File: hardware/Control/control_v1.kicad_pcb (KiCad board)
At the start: 2 copper layers, 109.2 x 88.9 mm, 40 parts, among them J1 Conn_02x07_Counter_Clockwise, J2 Screw_Terminal_01x05, J3 Conn_01x06, J4 RJ45, M1 STM32F4-DISCOVERY, U1 TL2575HV-ADJ, U2 TL2575HV-ADJ

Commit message: Updated to rev 2
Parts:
- C1: footprint Capacitor_SMD:CP_Elec_10x10.5 -> Capacitor_THT:CP_Radial_D10.0mm_P5.00mm
- C10, R5, R6: moved to B.Cu
- C2: value 1mF -> 100uF; footprint Capacitor_THT:CP_Radial_D16.0mm_P7.50mm -> Capacitor_THT:CP_Radial_D10.0mm_P5.00mm
- C3: footprint Capacitor_SMD:CP_Elec_8x10 -> Capacitor_THT:CP_Radial_D10.0mm_P5.00mm
- C4: footprint Capacitor_SMD:CP_Elec_10x10 -> Capacitor_THT:CP_Radial_D10.0mm_P5.00mm
- R2, R3: footprint Resistor_SMD:R_0603_1608Metric_Pad1.05x0.95mm_HandSolder -> Resistor_SMD:R_0805_2012Metric_Pad1.33x1.40mm_HandSolder
- moved C10 27.8 mm to (124.5, 89.2)
- moved R6 27.7 mm to (124.5, 92.8)
- moved R5 27.5 mm to (124.6, 85.1), turned to 0 degrees
- moved R11 18.0 mm to (176.1, 119.4)
- moved R12 18.0 mm to (176.1, 123.2)
- moved C8 18.0 mm to (176.1, 115.6)
- moved D1 12.6 mm to (165.0, 84.0), turned to 180 degrees
- moved C4 2.54 mm to (201.9, 125.7)
- moved C3 2.25 mm to (202.8, 95.5)
- moved C2 2.05 mm to (113.8, 119.6)
- moved L1 1.02 mm to (204.3, 79.8), turned to 0 degrees
- turned C5 to 0 degrees
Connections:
- MK1 pad 1: (no net) -> /GND
- MK2 pad 1: (no net) -> /GND
- MK3 pad 1: (no net) -> /GND
- MK4 pad 1: (no net) -> /GND
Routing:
- net /LS_A_TTL_PWM: track 24.8 -> 76.0 mm
- net /LS_C_TTL_PWM: track 20.5 -> 68.8 mm, vias 1 -> 0
- net /PHASEB_FB: track 70.6 -> 23.8 mm, vias 1 -> 2
- net /microcontroller/HALL_B_SENSE: track 22.9 -> 65.4 mm, vias 0 -> 1
- net /LS_B_TTL_PWM: track 31.7 -> 72.5 mm
- net /PHASEA_FB: track 41.1 -> 75.1 mm
- net /5v: track 271.3 -> 244.5 mm
- net /powerconverters/5v_OUT: track 56.3 -> 79.0 mm
- net /12v: track 142.2 -> 163.9 mm
- net /HALL_B: track 47.8 -> 34.4 mm
- net /microcontroller/PC5: track 27.0 -> 15.1 mm
- net /I2C_SCL: track 57.9 -> 68.6 mm, vias 1 -> 0
- net /48v: track 174.6 -> 183.7 mm, vias 4 -> 3
- net /powerconverters/12v_OUT: track 71.3 -> 79.8 mm, vias 1 -> 0
- net /GND: track 0.00 -> 7.19 mm, vias 9 -> 3
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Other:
- board text added: "Alex Simon 3/9/2019 Rev. 2"
- board text removed: "Alex Simon 2/7/2019 Rev. 1"

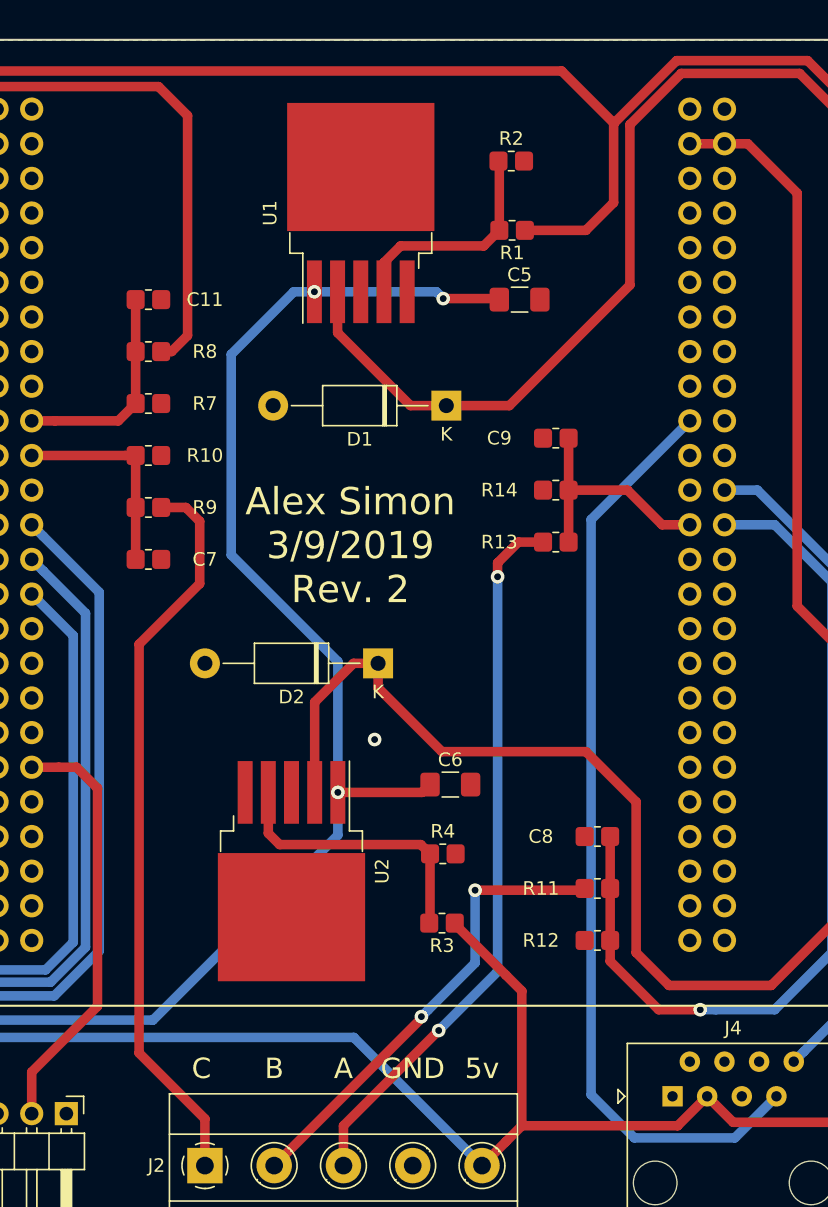
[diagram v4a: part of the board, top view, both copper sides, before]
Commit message: Added Transmission Enable
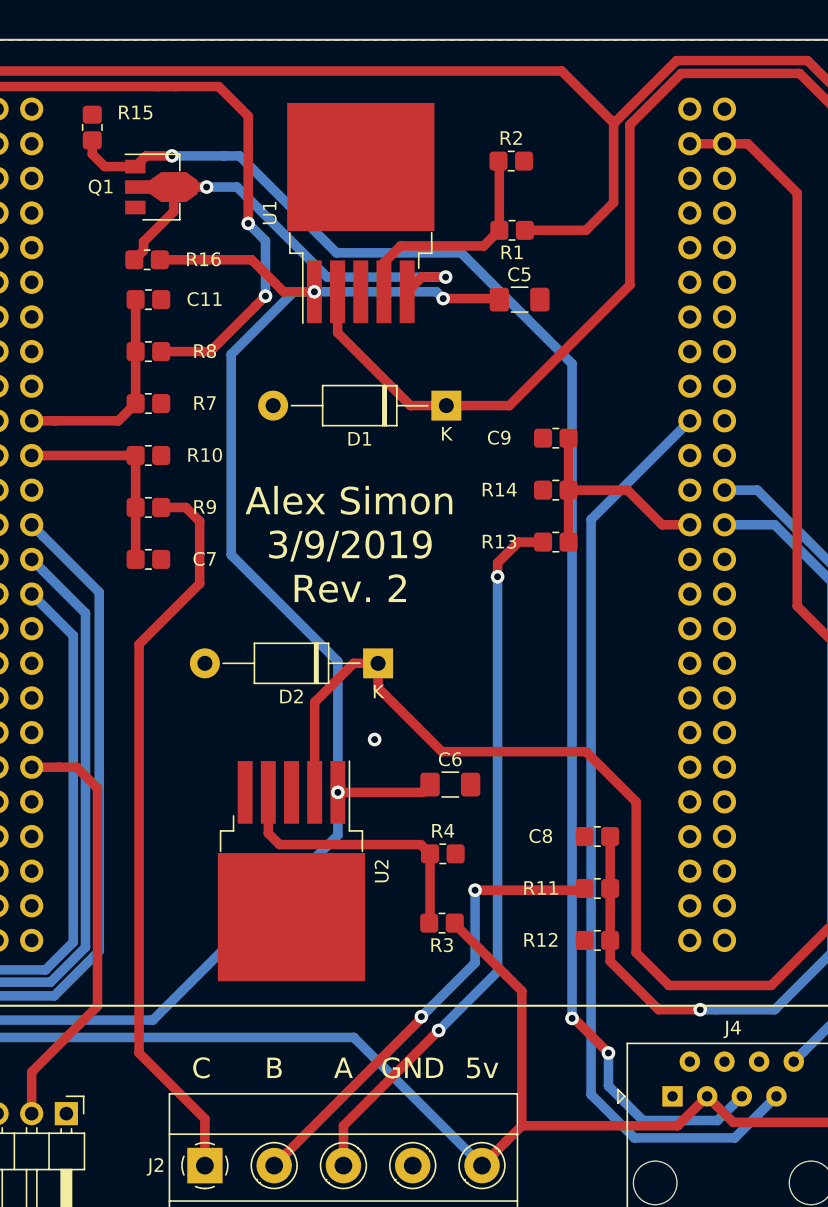
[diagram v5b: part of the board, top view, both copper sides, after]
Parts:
- added Q1: BCX56, Package_TO_SOT_SMD:SOT-89-3, F.Cu at (143.7, 67.9)
- added R15: 2k, Resistor_SMD:R_0805_2012Metric_Pad1.33x1.40mm_HandSolder, F.Cu at (139.1, 63.6)
- added R16: 18k, Resistor_SMD:R_0805_2012Metric_Pad1.33x1.40mm_HandSolder, F.Cu at (143.1, 73.3)
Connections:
- J3 pad 1: Net-(J3-Pad1) -> (no net)
- J3 pad 4: Net-(J3-Pad4) -> (no net)
- J3 pad 5: Net-(J3-Pad5) -> (no net)
- J4 pad 1: Net-(J4-Pad1) -> (no net)
- J4 pad 2: Net-(J4-Pad2) -> (no net)
- J4 pad 4: Net-(J4-Pad4) -> (no net)
- J4 pad 5: Net-(J4-Pad5) -> /TransEnable_TTL
- M1 pad 10: Net-(M1-Pad10) -> (no net)
- M1 pad 12: Net-(M1-Pad12) -> (no net)
- M1 pad 13: Net-(M1-Pad13) -> (no net)
- M1 pad 14: Net-(M1-Pad14) -> (no net)
- M1 pad 15: Net-(M1-Pad15) -> (no net)
- M1 pad 16: Net-(M1-Pad16) -> (no net)
- M1 pad 17: Net-(M1-Pad17) -> (no net)
- M1 pad 18: Net-(M1-Pad18) -> (no net)
- M1 pad 21: Net-(M1-Pad21) -> (no net)
- M1 pad 24: Net-(M1-Pad24) -> (no net)
- M1 pad 25: Net-(M1-Pad25) -> (no net)
- M1 pad 3: Net-(M1-Pad3) -> (no net)
- M1 pad 32: Net-(M1-Pad32) -> (no net)
- M1 pad 33: Net-(M1-Pad33) -> (no net)
- M1 pad 34: Net-(M1-Pad34) -> (no net)
- M1 pad 35: Net-(M1-Pad35) -> (no net)
- M1 pad 36: Net-(M1-Pad36) -> (no net)
- M1 pad 37: Net-(M1-Pad37) -> (no net)
- M1 pad 38: Net-(M1-Pad38) -> (no net)
- M1 pad 39: Net-(M1-Pad39) -> (no net)
- M1 pad 4: Net-(M1-Pad4) -> (no net)
- M1 pad 42: Net-(M1-Pad42) -> (no net)
- M1 pad 43: Net-(M1-Pad43) -> (no net)
- M1 pad 44: Net-(M1-Pad44) -> (no net)
- M1 pad 45: Net-(M1-Pad45) -> (no net)
- M1 pad 46: Net-(M1-Pad46) -> (no net)
- M1 pad 47: Net-(M1-Pad47) -> (no net)
- M1 pad 48: Net-(M1-Pad48) -> (no net)
- M1 pad 55: Net-(M1-Pad55) -> (no net)
- M1 pad 56: Net-(M1-Pad56) -> (no net)
- M1 pad 57: Net-(M1-Pad57) -> (no net)
- M1 pad 58: Net-(M1-Pad58) -> (no net)
- M1 pad 59: Net-(M1-Pad59) -> (no net)
- M1 pad 6: Net-(M1-Pad6) -> (no net)
- M1 pad 60: Net-(M1-Pad60) -> (no net)
- M1 pad 61: Net-(M1-Pad61) -> (no net)
- M1 pad 62: Net-(M1-Pad62) -> (no net)
- M1 pad 63: Net-(M1-Pad63) -> (no net)
- M1 pad 64: Net-(M1-Pad64) -> (no net)
- M1 pad 65: Net-(M1-Pad65) -> (no net)
- M1 pad 66: Net-(M1-Pad66) -> (no net)
- M1 pad 67: Net-(M1-Pad67) -> (no net)
- M1 pad 68: Net-(M1-Pad68) -> (no net)
- M1 pad 7: Net-(M1-Pad7) -> (no net)
- M1 pad 70: Net-(M1-Pad70) -> (no net)
- M1 pad 71: Net-(M1-Pad71) -> (no net)
- M1 pad 72: Net-(M1-Pad72) -> (no net)
- M1 pad 73: Net-(M1-Pad73) -> (no net)
- M1 pad 77: Net-(M1-Pad77) -> (no net)
- M1 pad 78: Net-(M1-Pad78) -> (no net)
- M1 pad 79: Net-(M1-Pad79) -> (no net)
- M1 pad 8: Net-(M1-Pad8) -> (no net)
- M1 pad 80: Net-(M1-Pad80) -> (no net)
- M1 pad 81: Net-(M1-Pad81) -> (no net)
- M1 pad 82: Net-(M1-Pad82) -> (no net)
- M1 pad 83: Net-(M1-Pad83) -> (no net)
- M1 pad 84: Net-(M1-Pad84) -> (no net)
- M1 pad 85: Net-(M1-Pad85) -> (no net)
- M1 pad 86: Net-(M1-Pad86) -> (no net)
- M1 pad 87: Net-(M1-Pad87) -> (no net)
- M1 pad 88: Net-(M1-Pad88) -> (no net)
- M1 pad 89: Net-(M1-Pad89) -> (no net)
- M1 pad 90: Net-(M1-Pad90) -> (no net)
- M1 pad 91: Net-(M1-Pad91) -> (no net)
- M1 pad 92: Net-(M1-Pad92) -> (no net)
- M1 pad 93: Net-(M1-Pad93) -> (no net)
- M1 pad 94: Net-(M1-Pad94) -> (no net)
- M1 pad 95: Net-(M1-Pad95) -> (no net)
- M1 pad 96: Net-(M1-Pad96) -> (no net)
- M1 pad 97: Net-(M1-Pad97) -> (no net)
- M1 pad 98: Net-(M1-Pad98) -> (no net)
- U1 pad 5: /GND -> /powerconverters/TransEnable
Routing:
- net /TransEnable_TTL: track 0.00 -> 109.3 mm, vias 0 -> 3
- net /powerconverters/TransEnable: track 0.00 -> 35.1 mm, vias 0 -> 2
- net /48v: track 183.7 -> 196.0 mm
- net /PHASEA_FB: track 75.1 -> 84.1 mm, vias 0 -> 2

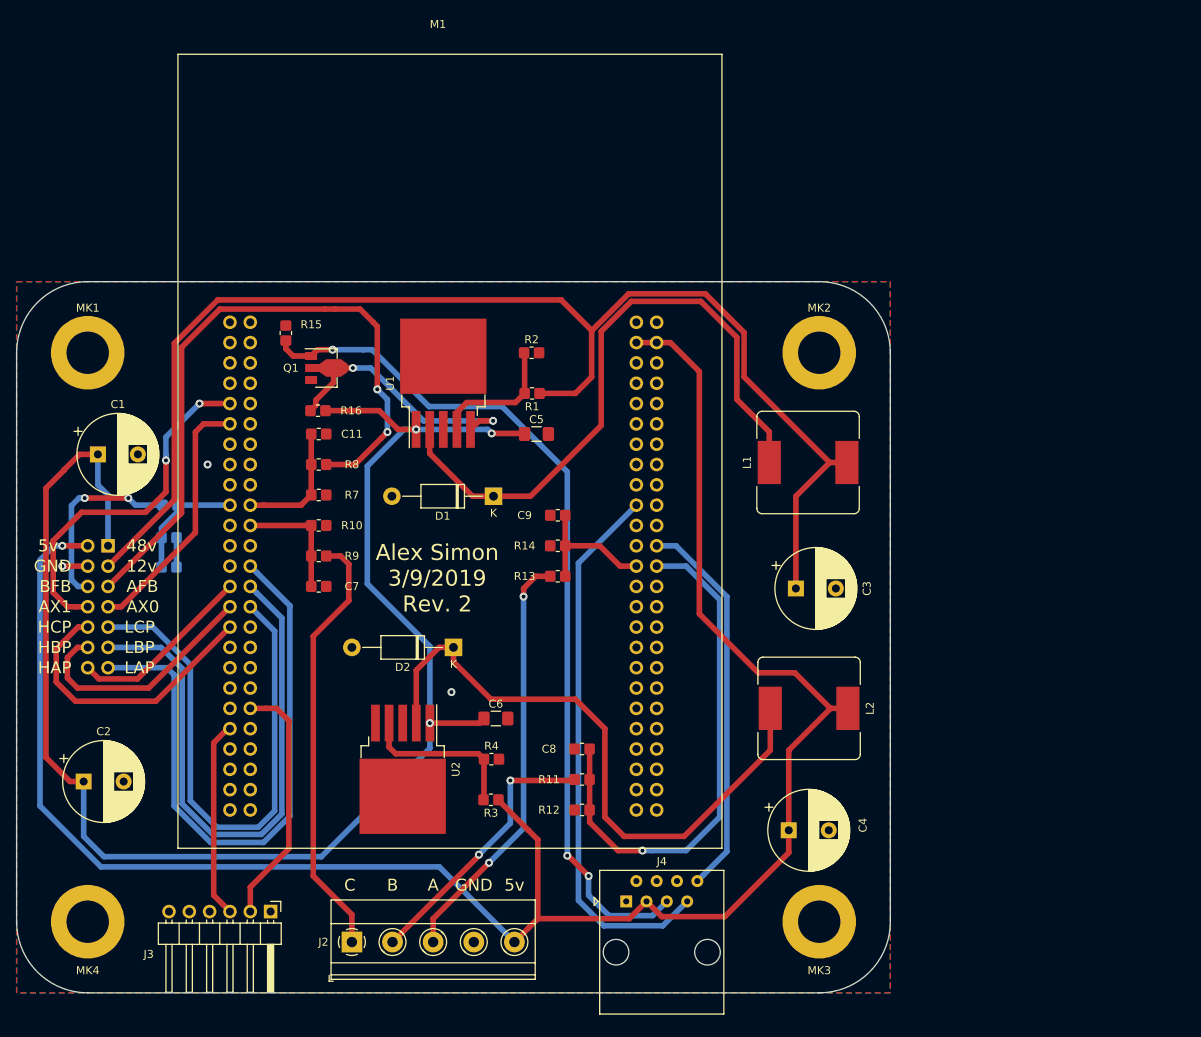
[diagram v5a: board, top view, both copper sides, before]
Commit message: Added RS485 differential pair
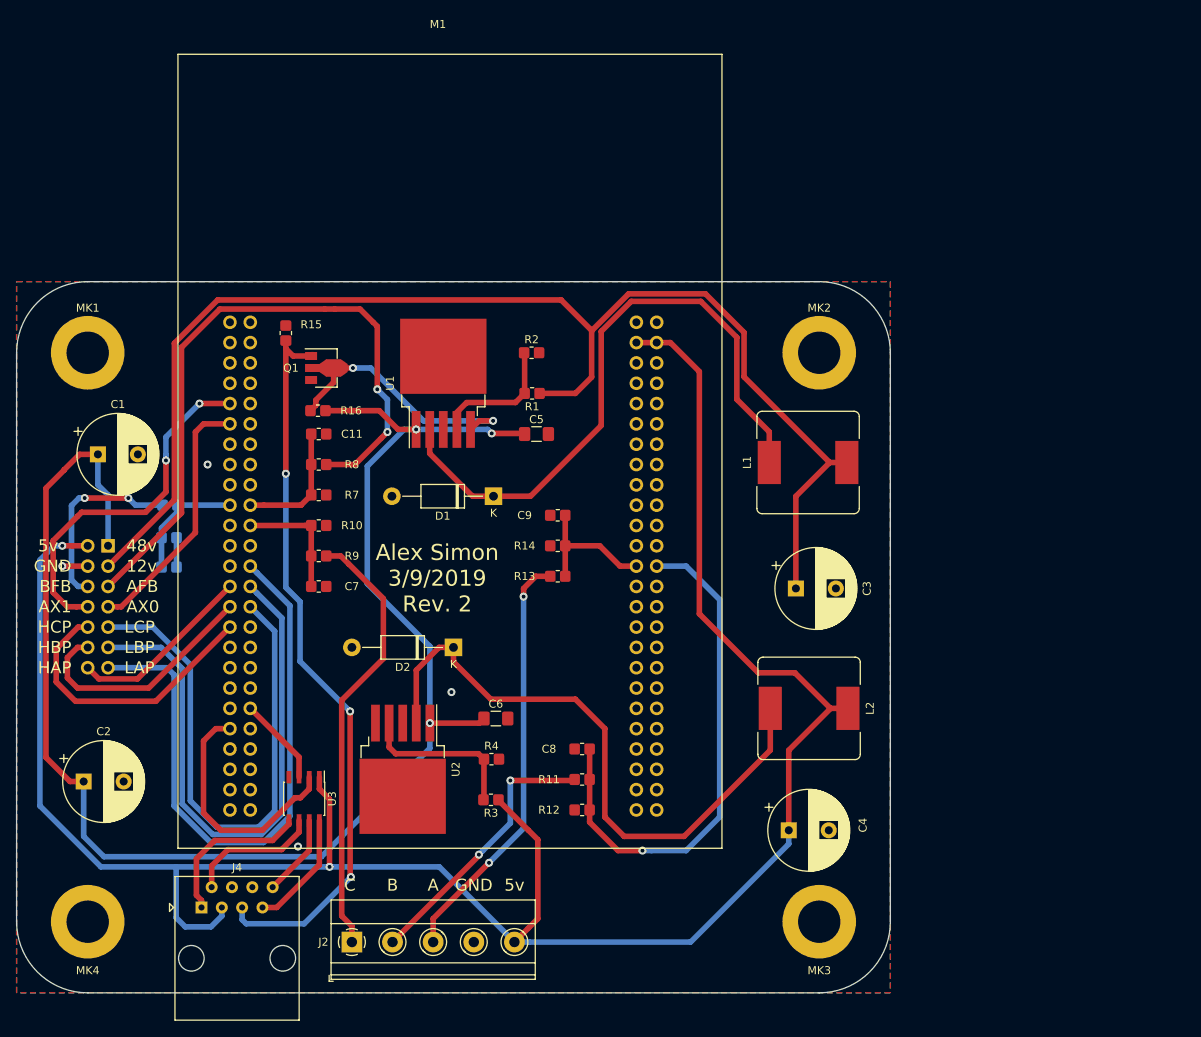
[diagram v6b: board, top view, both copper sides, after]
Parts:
- removed J3: Conn_01x06, Connector_PinHeader_2.54mm:PinHeader_1x06_P2.54mm_Horizontal
- added U3: DS89C21, Package_SO:SOIC-8_3.9x4.9mm_P1.27mm, F.Cu at (141.4, 121.8)
- moved J4 53.1 mm to (128.5, 135.4)
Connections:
- J4 pad 1: (no net) -> /-TX
- J4 pad 2: (no net) -> /+TX
- J4 pad 7: /I2C_SCL -> /+RX
- J4 pad 8: /I2C_SDA -> /-RX
- M1 pad 69: /I2C_SCL -> (no net)
- M1 pad 74: /I2C_SDA -> (no net)
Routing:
- net /I2C_SCL: track 68.6 -> 0.00 mm
- net /I2C_SDA: track 48.5 -> 0.00 mm
- net /5v: track 244.5 -> 272.3 mm, vias 1 -> 2
- net /USART_TX: track 31.3 -> 11.1 mm
- net /-TX: track 0.00 -> 20.2 mm
- net /TransEnable_TTL: track 109.3 -> 92.1 mm
- net /+TX: track 0.00 -> 16.8 mm
- net /+RX: track 0.00 -> 14.9 mm
- net /-RX: track 0.00 -> 10.2 mm
- net /USART_RX: track 24.7 -> 30.9 mm
- net /HALL_C: track 54.3 -> 55.0 mm
- net /GND: vias 3 -> 4

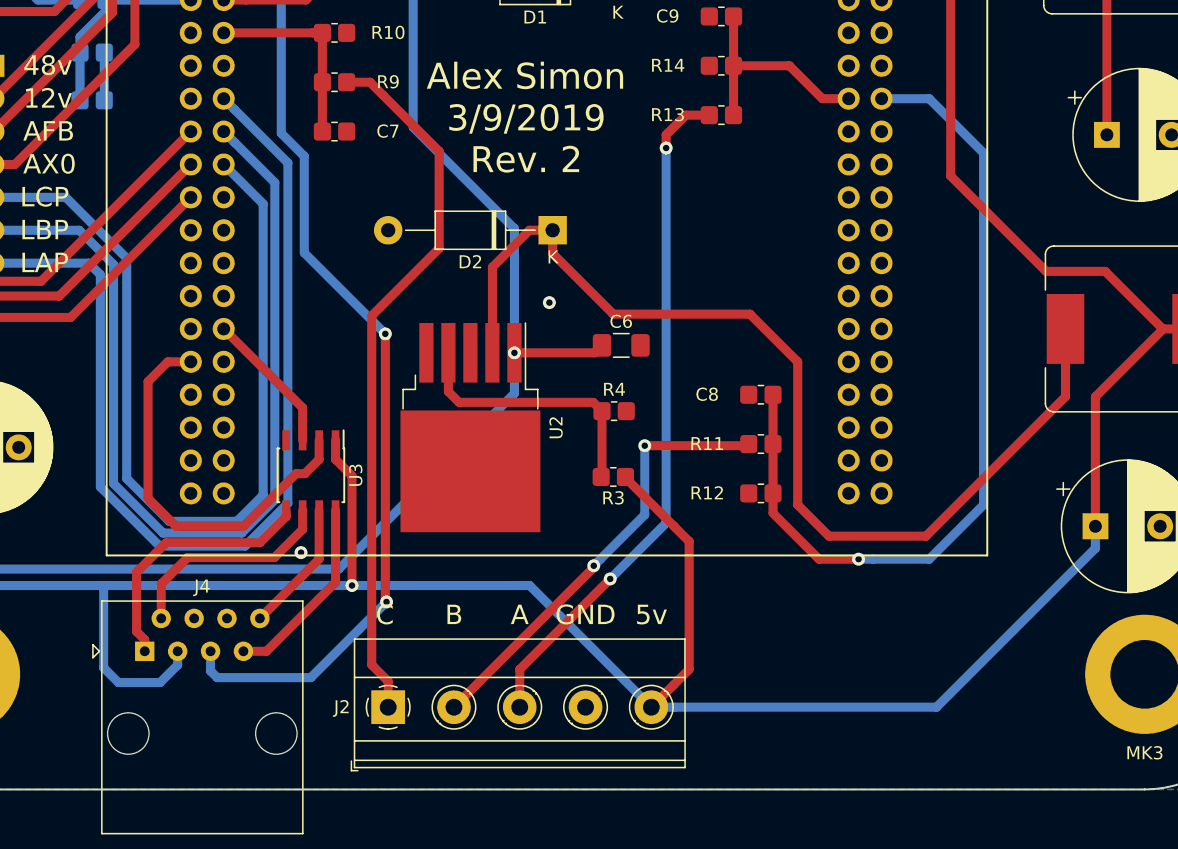
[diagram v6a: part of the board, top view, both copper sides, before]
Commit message: Added termination resistors
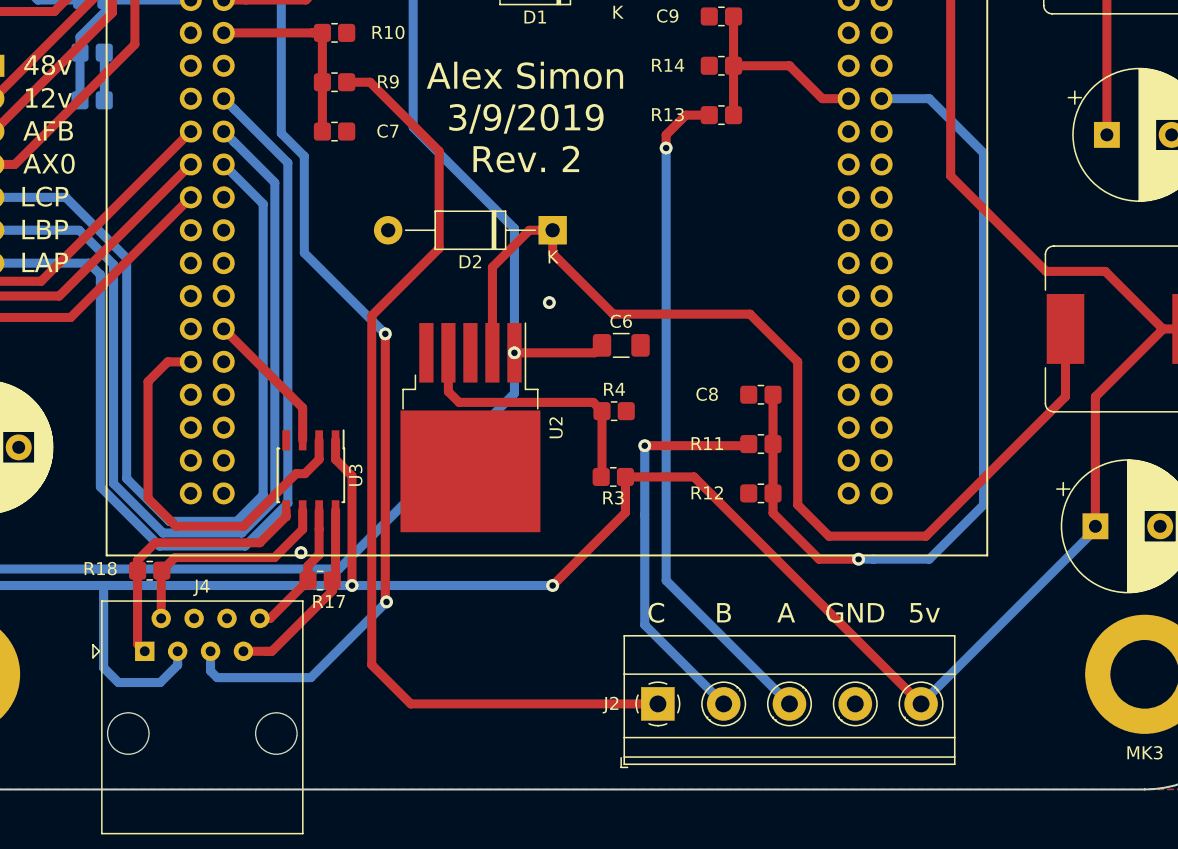
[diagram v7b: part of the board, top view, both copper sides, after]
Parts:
- added R17: 120, Resistor_SMD:R_0805_2012Metric_Pad1.33x1.40mm_HandSolder, F.Cu at (142.1, 129.9)
- added R18: 120, Resistor_SMD:R_0805_2012Metric_Pad1.33x1.40mm_HandSolder, F.Cu at (128.9, 129.2)
- moved J2 20.8 mm to (168.1, 139.4)
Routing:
- net /HALL_C: track 55.0 -> 74.5 mm
- net /5v: track 272.3 -> 259.1 mm, vias 2 -> 3
- net /HALL_B: track 34.4 -> 30.5 mm, vias 2 -> 1
- net /HALL_A: track 52.8 -> 51.9 mm, vias 2 -> 1
- net /+TX: track 16.8 -> 17.4 mm
